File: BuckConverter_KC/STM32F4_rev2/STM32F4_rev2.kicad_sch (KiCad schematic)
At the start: 3 parts

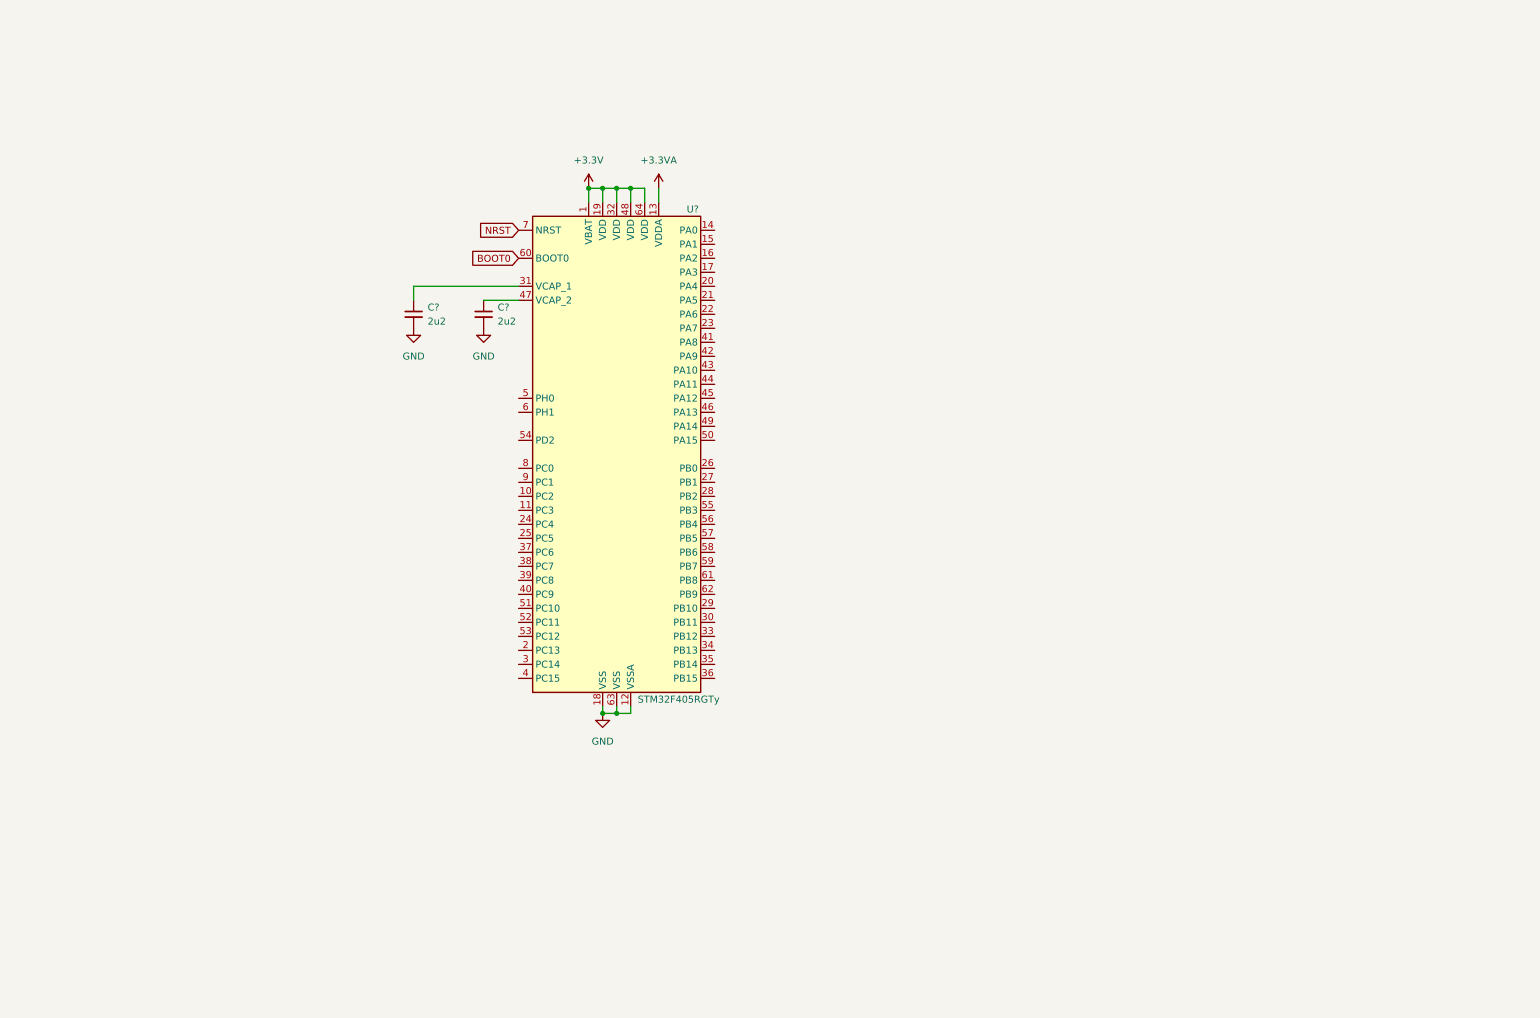
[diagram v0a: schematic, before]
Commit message: finished stm32, power and basic connector schematic; added parts in library; deleted backup files
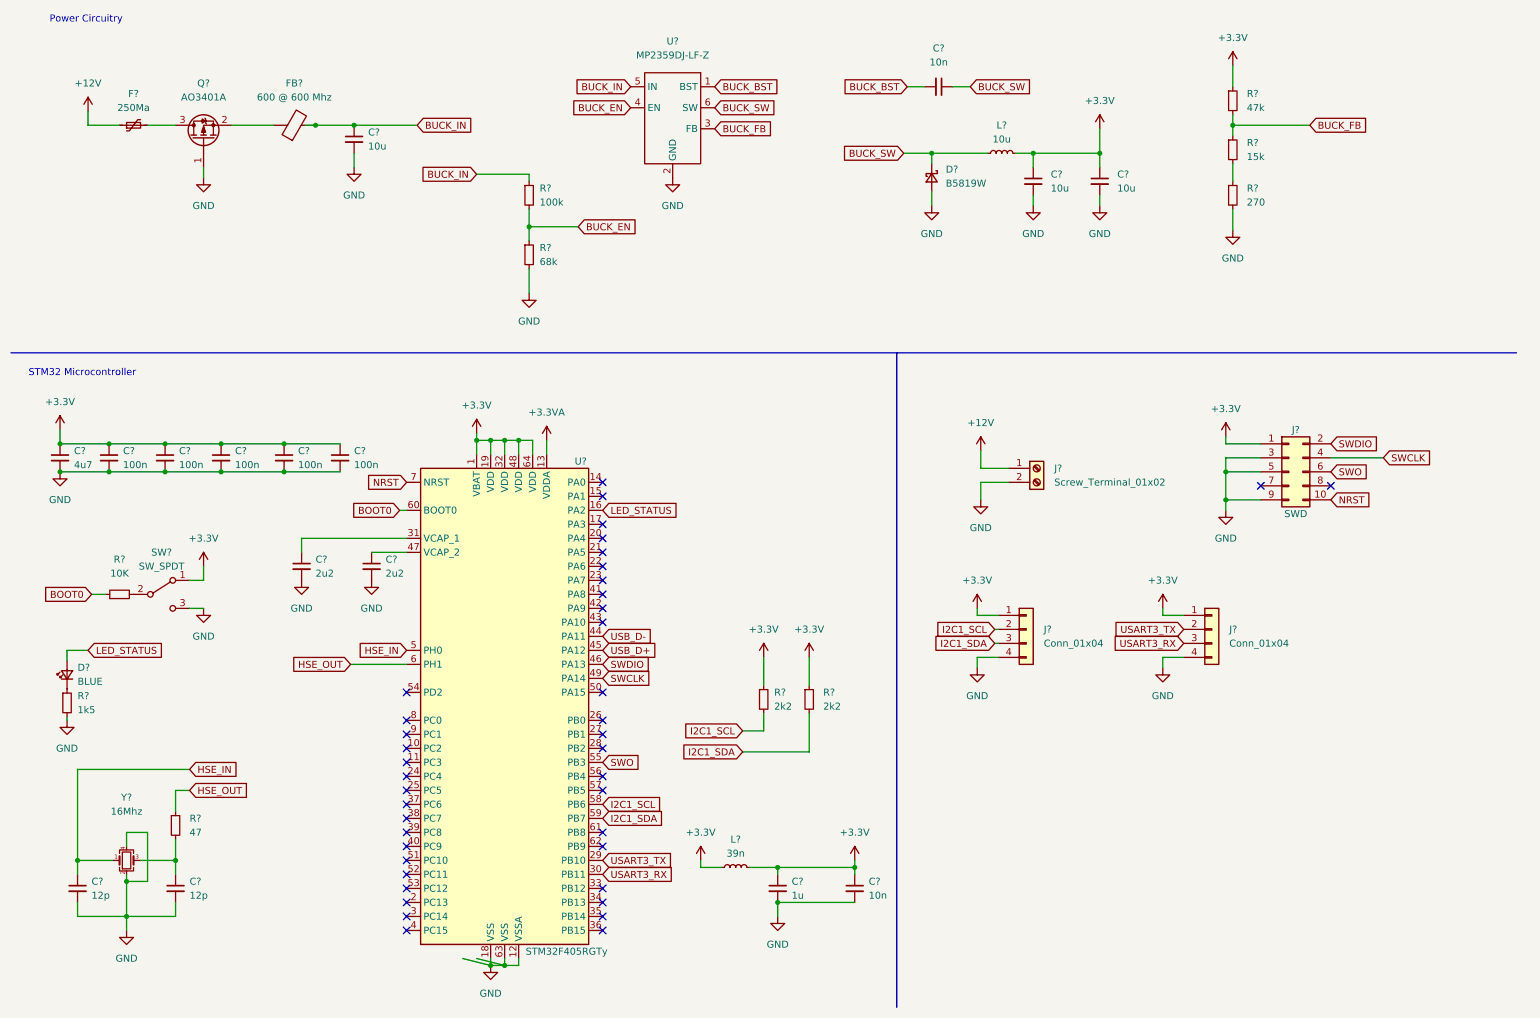
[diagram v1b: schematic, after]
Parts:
- added C? (x3): 10u, symbol Device:C_Small
- added C? (x2): 10n, symbol Device:C_Small
- added C? (x2): 12p, symbol Device:C_Small
- added C?: 1u, symbol Device:C_Small
- added C? (x5): 100n, symbol Device:C_Small
- added C?: 4u7, symbol Device:C_Small
- added D?: B5819W, symbol Device:D_Schottky_Small
- added D?: BLUE, symbol Device:LED_Small
- added F?: 250Ma, symbol Device:Polyfuse_Small
- added FB?: 600 @ 600 Mhz, symbol Device:FerriteBead
- added J?: Screw_Terminal_01x02, symbol Connector:Screw_Terminal_01x02
- added J? (x2): Conn_01x04, symbol Connector_Generic:Conn_01x04
- added J?: SWD, symbol Connector_Generic:Conn_02x05_Odd_Even
- added L?: 10u, symbol Device:L_Small
- added L?: 39n, symbol Device:L_Small
- added Q?: AO3401A, Package_TO_SOT_SMD:SOT-23, symbol Transistor_FET:AO3401A
- added R?: 270, symbol Device:R_Small
- added R? (x2): 2k2, symbol Device:R_Small
- added R?: 10K, symbol Device:R_Small
- added R?: 47, symbol Device:R_Small
- added R?: 100k, symbol Device:R_Small
- added R?: 1k5, symbol Device:R_Small
- added R?: 15k, symbol Device:R_Small
- added R?: 47k, symbol Device:R_Small
- added R?: 68k, symbol Device:R_Small
- added SW?: SW_SPDT, symbol Switch:SW_SPDT
- added U?: MP2359DJ-LF-Z, symbol Misc:MP2359DJ-LF-Z
- added Y?: 16Mhz, symbol Device:Crystal_GND24_Small
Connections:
- net +3.3V: now also C?.1, C?.1, C?.1, C?.1, C?.1, C?.1, C?.1, C?.1, C?.1, C?.1, J?.1 (Pin_1), J?.1 (Pin_1), J?.1 (Pin_1), L?.1, L?.2, L?.2, R?.1, R?.1, R?.1, SW?.1 (A)
- net BOOT0: now also R?.1
- net GND: now also C?.2, C?.2, C?.2, C?.2, C?.2, C?.2, C?.2, C?.2, C?.2, C?.2, C?.2, C?.2, C?.2, D?.2 (A), J?.2 (Pin_2), J?.3 (Pin_3), J?.4 (Pin_4), J?.4 (Pin_4), J?.5 (Pin_5), J?.9 (Pin_9), Q?.1 (G), R?.2, R?.2, R?.2, SW?.3 (C), U?.2 (GND), Y?.2, Y?.4
- net NRST: now also J?.10 (Pin_10)
- net LED_STATUS: now reaches U?.16 (PA2)
- net LED_STATUS: now also D?.2 (A)
- net USART3_TX: now reaches U?.29 (PB10)
- net USART3_TX: now also J?.2 (Pin_2)
- net USART3_RX: now reaches U?.30 (PB11)
- net USART3_RX: now also J?.3 (Pin_3)
- net USB_D-: now reaches U?.44 (PA11)
- net USB_D+: now reaches U?.45 (PA12)
- net SWDIO: now reaches U?.46 (PA13)
- net SWDIO: now also J?.2 (Pin_2)
- net SWCLK: now reaches U?.49 (PA14)
- net SWCLK: now also J?.4 (Pin_4)
- net HSE_IN: now reaches U?.5 (PH0)
- net HSE_IN: now also C?.1, Y?.1
- net SWO: now reaches U?.55 (PB3)
- net SWO: now also J?.6 (Pin_6)
- net I2C1_SCL: now reaches U?.58 (PB6)
- net I2C1_SCL: now also J?.2 (Pin_2), R?.2
- net I2C1_SDA: now reaches U?.59 (PB7)
- net I2C1_SDA: now also J?.3 (Pin_3), R?.2
- net HSE_OUT: now reaches U?.6 (PH1)
- net HSE_OUT: now also R?.1
- new net: C?.1, R?.2, Y?.3
- new net: R?.1, R?.2
- new net: R?.2, SW?.2 (B)
- new net: D?.1 (K), R?.1
- new net: F?.2, Q?.3 (D)
- new net: FB?.1, Q?.2 (S)
- new net +12V: F?.1, J?.1 (Pin_1)
- new net BUCK_BST: C?.2, U?.1 (BST)
- new net BUCK_EN: R?.1, R?.2, U?.4 (EN)
- new net BUCK_FB: R?.1, R?.2, U?.3 (FB)
- new net BUCK_IN: C?.1, FB?.2, R?.1, U?.5 (IN)
- new net BUCK_SW: C?.1, D?.1 (K), L?.1, U?.6 (SW)
- no-connect marks 0 -> 41
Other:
- note added: "Power Circuitry"
- note added: "STM32 Microcontroller"
- moved on the sheet: C?, U?

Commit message: finished schematic (added usb, mounting holes, add labels); started layout
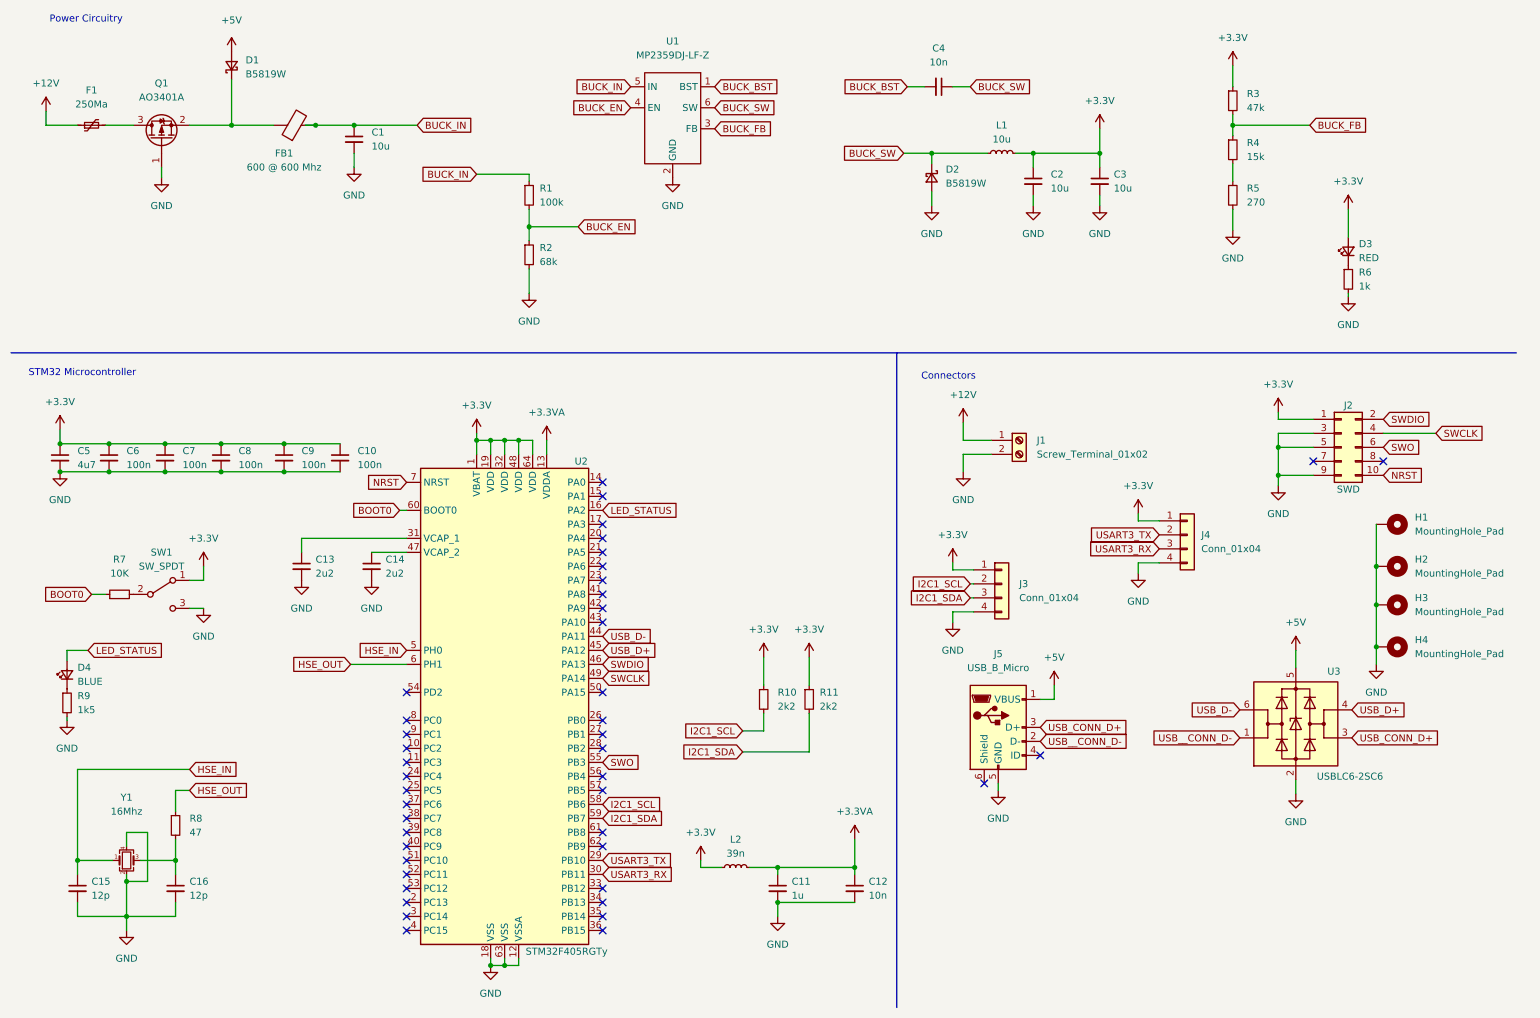
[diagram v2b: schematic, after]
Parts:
- added D1: B5819W, Diode_SMD:D_SOD-123, symbol Device:D_Schottky_Small
- added D3: RED, Diode_SMD:D_0603_1608Metric, symbol Device:LED_Small
- added H1, H2, H3, H4: MountingHole_Pad, MountingHole:MountingHole_4.3mm_M4_Pad_Via, symbol Mechanical:MountingHole_Pad
- added J5: USB_B_Micro, Connector_USB:USB_Micro-B_Amphenol_10103594-0001LF_Horizontal, symbol Connector:USB_B_Micro
- added R6: 1k, Resistor_SMD:R_0603_1608Metric, symbol Device:R_Small
- added U3: USBLC6-2SC6, Package_TO_SOT_SMD:SOT-23-6, symbol Power_Protection:USBLC6-2SC6
- C1, C2, C3: renamed from C?; footprint (none) -> Capacitor_SMD:C_1206_3216Metric
- C10, C11, C12, C15, C16, C6, C7, C8, C9: renamed from C?; footprint (none) -> Capacitor_SMD:C_0402_1005Metric
- C13, C14, C4, C5: renamed from C?; footprint (none) -> Capacitor_SMD:C_0603_1608Metric
- D2: renamed from D?; footprint (none) -> Diode_SMD:D_SOD-123
- D4: renamed from D?; footprint (none) -> Diode_SMD:D_0603_1608Metric
- F1: renamed from F?; footprint (none) -> Fuse:Fuse_1206_3216Metric
- FB1: renamed from FB?; footprint (none) -> Inductor_SMD:L_0805_2012Metric
- J1: renamed from J?; footprint (none) -> TerminalBlock_Phoenix:TerminalBlock_Phoenix_PT-1,5-2-3.5-H_1x02_P3.50mm_Horizontal
- J2: renamed from J?; footprint (none) -> Connector_PinSocket_1.27mm:PinSocket_2x05_P1.27mm_Vertical_SMD
- J3, J4: renamed from J?; footprint (none) -> Connector_Molex:Molex_PicoBlade_53048-0410_1x04_P1.25mm_Horizontal
- L1: renamed from L?; footprint (none) -> Inductor_SMD:L_Sunlord_MWSA0518_5.4x5.2mm
- L2: renamed from L?; footprint (none) -> Inductor_SMD:L_0402_1005Metric
- R1, R2, R3, R4, R5, R9: renamed from R?; footprint (none) -> Resistor_SMD:R_0603_1608Metric
- R10, R11, R7, R8: renamed from R?; footprint (none) -> Resistor_SMD:R_0402_1005Metric
- SW1: renamed from SW?; footprint (none) -> Button_Switch_SMD:SW_SPDT_PCM12
- U1: renamed from U?; footprint (none) -> Package_TO_SOT_SMD:SOT-23-6
- Y1: renamed from Y?; footprint (none) -> Crystal:Crystal_SMD_3225-4Pin_3.2x2.5mm
- gave numbers to parts that had none: 2
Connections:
- net +3.3V: now also D3.2 (A); no longer C11.1, C12.1, L2.2
- net +3.3VA: now also C11.1, C12.1, L2.2
- net GND: now also H1.1, H2.1, H3.1, H4.1, J5.5 (GND), R6.2, U3.2 (GND)
- net USB_D+: now also U3.4 (I/O2)
- net USB_D-: now also U3.6 (I/O1)
- net at FB1.1, Q1.2 (S): now also D1.1 (K)
- new net: D3.1 (K), R6.1
- new net +5V: D1.2 (A), J5.1 (VBUS), U3.5 (VBUS)
- new net USB_CONN_D+: J5.3 (D+), U3.3 (I/O2)
- new net USB__CONN_D-: J5.2 (D-), U3.1 (I/O1)
- no-connect marks 41 -> 43
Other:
- note added: "Connectors"
- moved on the sheet: F1, J1, J2, J3, J4, Q1
